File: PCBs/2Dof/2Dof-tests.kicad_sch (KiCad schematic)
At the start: 50 parts, among them J1 Conn_02x07_Odd_Even, J12 RS485, J14 HBA, J17 Servo1, J2 Conn_02x08_Odd_Even, J3 Conn_02x08_Odd_Even, J5 24Vin, J9 Laser Diode, Q1 QServoA, Q6 LaserDiodeT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

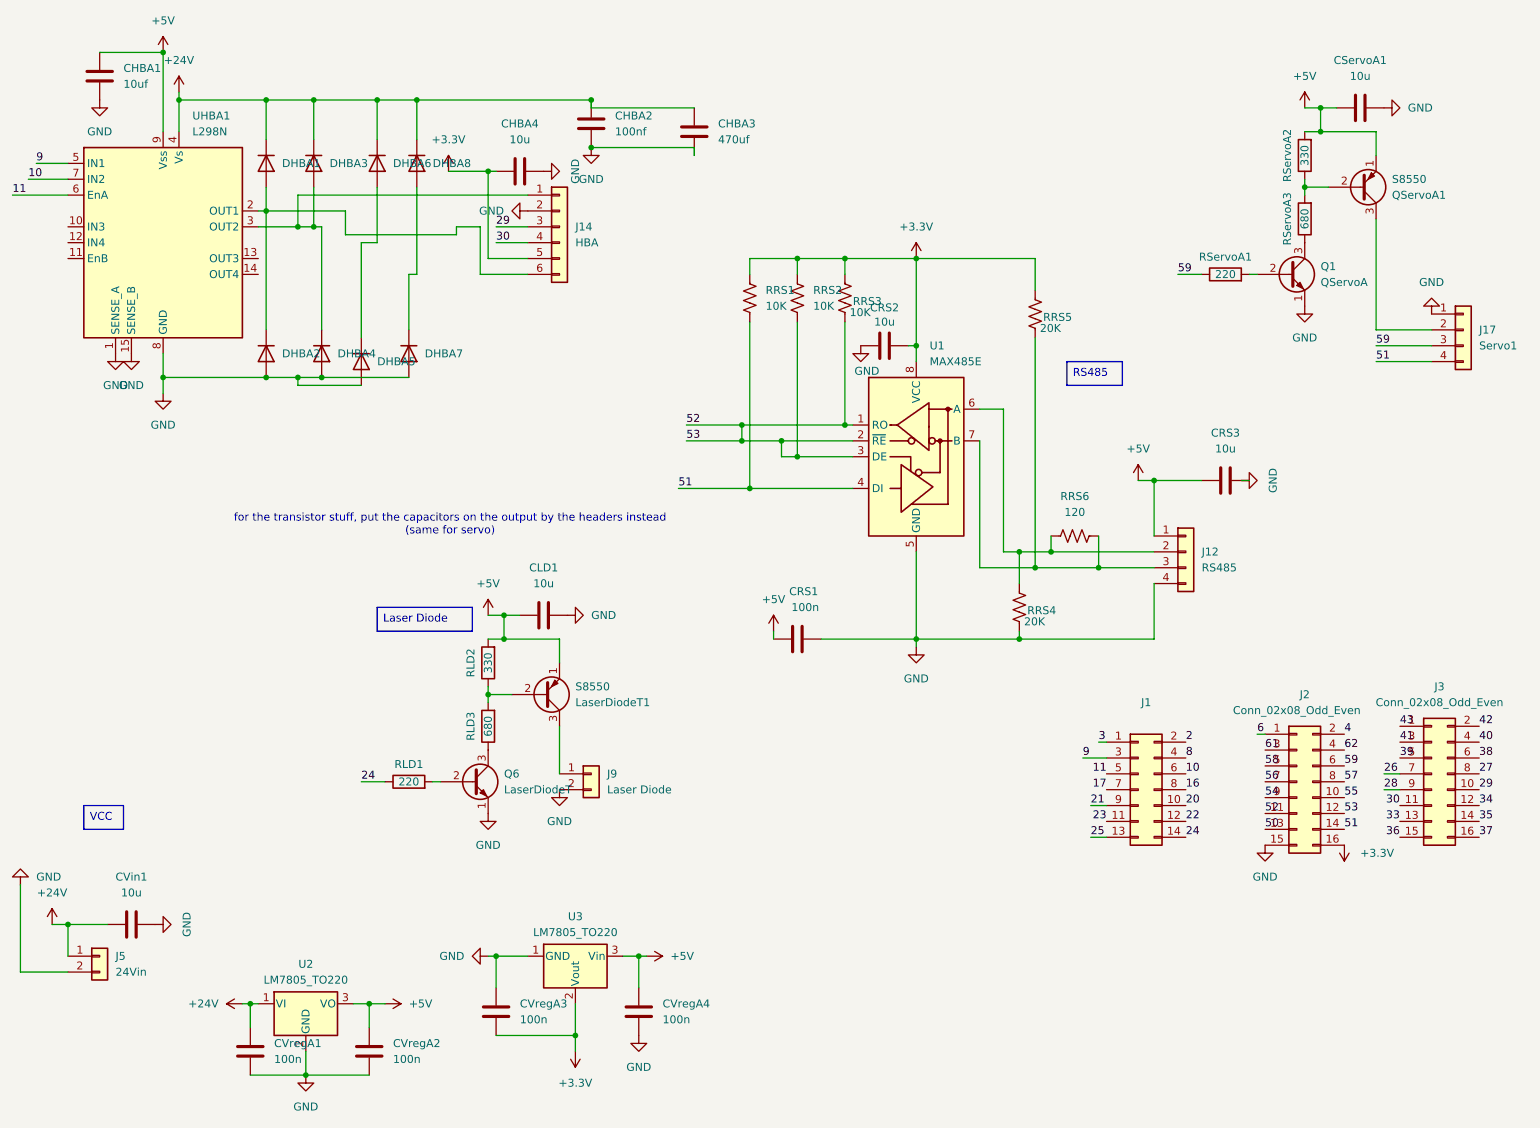
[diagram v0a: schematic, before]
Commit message: 2dof changes, cleaned up routing, fixed vias
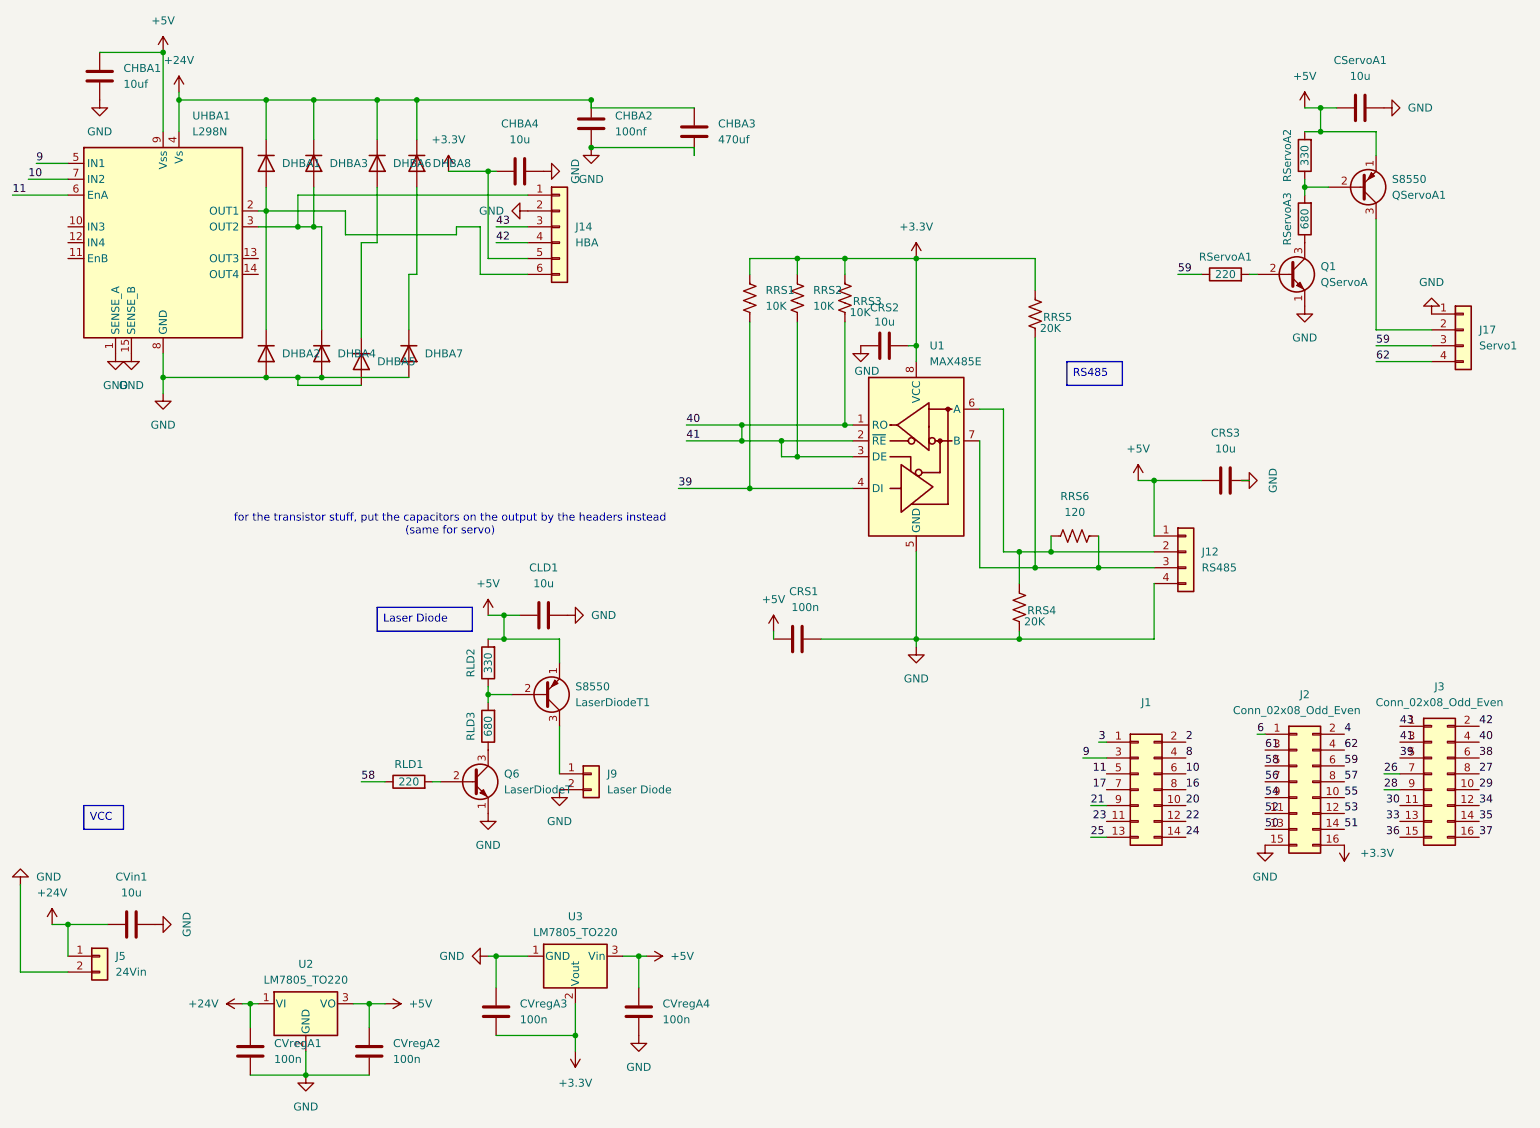
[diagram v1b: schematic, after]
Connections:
- net 41 is gone; now on net 40: J3.3 (Pin_3)
- net 24: no longer RLD1.1
- net 29: no longer J14.3 (Pin_3)
- net 30: no longer J14.4 (Pin_4)
- net 39: now also RRS1.2, U1.4 (DI)
- net 40: now also RRS2.2, RRS3.2, U1.1 (RO), U1.2 (~{RE}), U1.3 (DE)
- net 42: now also J14.4 (Pin_4)
- net 43: now also J14.3 (Pin_3)
- net 51: no longer J17.4 (Pin_4), RRS1.2, U1.4 (DI)
- net 52: no longer J2.12 (Pin_12), RRS2.2, RRS3.2, U1.1 (RO), U1.2 (~{RE}), U1.3 (DE)
- net 58: now also RLD1.1
- net 62: now also J17.4 (Pin_4)
- new net 53: J2.12 (Pin_12)
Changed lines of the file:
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@@
 		)
 	)
-	(label "52"
+	(label "40"
 		(at 139.7 82.55 0)
 		(effects
@@
 		)
 	)
-	(label "53"
+	(label "41"
 		(at 139.7 85.09 0)
 		(effects
@@
 		)
 	)
-	(label "51"
+	(label "62"
 		(at 250.19 72.39 0)
 		(effects
@@
 		)
 	)
-	(label "51"
+	(label "39"
 		(at 138.43 92.71 0)
 		(effects
@@
 		)
 	)
-	(label "29"
+	(label "43"
 		(at 109.22 50.8 0)
 		(effects
@@
 		)
 	)
-	(label "24"
+	(label "58"
 		(at 87.63 139.7 0)
 		(effects
@@
 		)
 	)
-	(label "30"
+	(label "42"
 		(at 109.22 53.34 0)
 		(effects

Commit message: small fixes + comments
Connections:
- net 33: now also RRS3.2, U1.1 (RO)
- net 35: now also RRS1.2, U1.4 (DI)
- net 39: no longer RRS1.2, U1.4 (DI)
- net 40: no longer J3.3 (Pin_3), RRS2.2, RRS3.2, U1.1 (RO), U1.2 (~{RE}), U1.3 (DE)
- net 50: now also J17.3 (Pin_3)
- net 52: now also J17.4 (Pin_4)
- net 59: no longer J17.3 (Pin_3)
- net 62: no longer J17.4 (Pin_4)
- new net 41: J3.3 (Pin_3), RRS2.2, U1.2 (~{RE}), U1.3 (DE)
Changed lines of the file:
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@@
-	)
-	(junction
-		(at 148.59 82.55)
-		(diameter 0)
-		(color 0 0 0 0)
 	)
 	(junction
@@
 	)
 	(junction
-		(at 148.59 85.09)
-		(diameter 0)
-		(color 0 0 0 0)
-	)
-	(junction
 		(at 110.49 113.03)
 		(diameter 0)
@@
 	(wire
 		(pts
-			(xy 139.7 82.55) (xy 148.59 82.55)
-		)
-		(stroke
-			(width 0)
-			(type default)
-		)
-	)
-	(wire
-		(pts
 			(xy 71.12 50.8) (xy 77.47 50.8)
 		)
@@
 	(wire
 		(pts
-			(xy 139.7 85.09) (xy 148.59 85.09)
-		)
-		(stroke
-			(width 0)
-			(type default)
-		)
-	)
-	(wire
-		(pts
 			(xy 31.75 45.72) (xy 40.64 45.72)
 		)
@@
 	(wire
 		(pts
-			(xy 148.59 82.55) (xy 165.1 82.55)
+			(xy 139.7 82.55) (xy 165.1 82.55)
 		)
 		(stroke
@@
 	(wire
 		(pts
-			(xy 148.59 82.55) (xy 148.59 85.09)
-		)
-		(stroke
-			(width 0)
-			(type default)
-		)
-	)
-	(wire
-		(pts
 			(xy 96.52 30.48) (xy 90.17 30.48)
 		)
@@
 	(wire
 		(pts
-			(xy 148.59 85.09) (xy 154.94 85.09)
+			(xy 139.7 85.09) (xy 154.94 85.09)
 		)
 		(stroke
@@
 		)
 	)
-	(label "40"
+	(label "33"
 		(at 139.7 82.55 0)
 		(effects
@@
 		)
 	)
-	(label "59"
+	(label "50"
 		(at 250.19 69.85 0)
 		(effects
@@
 		)
 	)
-	(label "62"
+	(label "52"
 		(at 250.19 72.39 0)
 		(effects
@@
 		)
 	)
-	(label "39"
+	(label "35"
 		(at 138.43 92.71 0)
 		(effects

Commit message: RS485 fixes
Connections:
- net 33: now also RRS1.2, U1.4 (DI); no longer RRS3.2, U1.1 (RO)
- net 35: now also RRS3.2, U1.1 (RO); no longer RRS1.2, U1.4 (DI)
- net 50: now also RServoA1.1
- net 59: no longer RServoA1.1
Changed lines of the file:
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@@
 		)
 	)
-	(label "33"
+	(label "35"
 		(at 139.7 82.55 0)
 		(effects
@@
 		)
 	)
-	(label "35"
+	(label "33"
 		(at 138.43 92.71 0)
 		(effects
@@
 		)
 	)
-	(label "59"
+	(label "50"
 		(at 218.44 58.42 0)
 		(effects

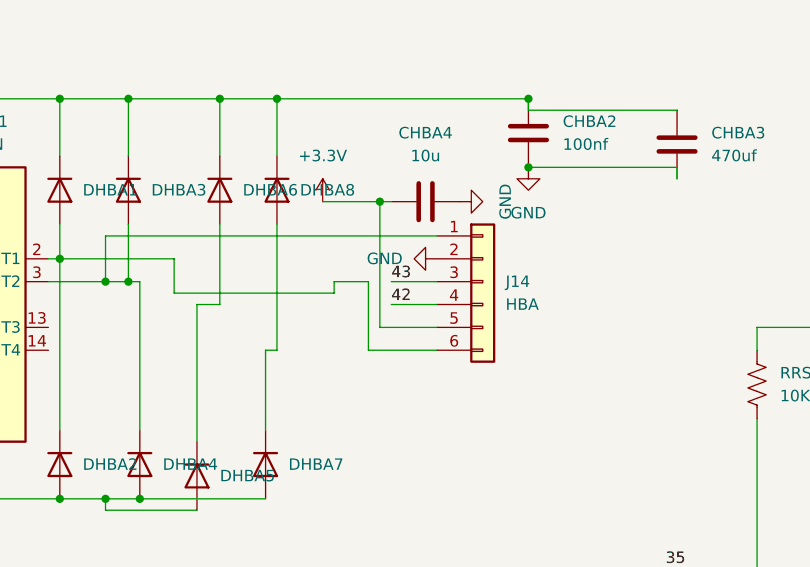
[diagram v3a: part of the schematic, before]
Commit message: minor silkscreen fixes
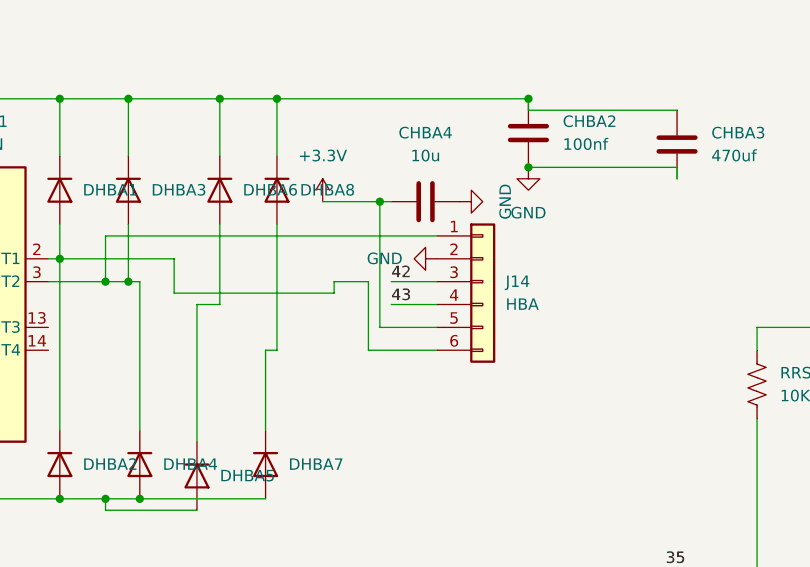
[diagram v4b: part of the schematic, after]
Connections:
- net 42: now also J14.3 (Pin_3); no longer J14.4 (Pin_4)
- net 43: now also J14.4 (Pin_4); no longer J14.3 (Pin_3)
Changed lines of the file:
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@@
 		)
 	)
-	(label "43"
+	(label "42"
 		(at 109.22 50.8 0)
 		(effects
@@
 		)
 	)
-	(label "42"
+	(label "43"
 		(at 109.22 53.34 0)
 		(effects

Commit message: diode fixes
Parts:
- removed DHBA5, DHBA6, DHBA7, DHBA8: 1N4148WT, Diode_SMD:D_SOD-123, symbol Diode:1N4148WT
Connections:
- net +24V: now also CVin1.2; no longer CVin1.1
- net GND: now also CVin1.1; no longer CVin1.2
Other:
- moved on the sheet: CVin1
